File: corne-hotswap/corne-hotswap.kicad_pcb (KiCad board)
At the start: 2 copper layers, 133.8 x 91.7 mm, 49 parts, among them J1 Battery Connector, J2 nice!view, J3 USB_C_Receptacle_PowerOnly_6P, J4 Battery Wire, SW1 SW_Push, SW10 SW_Push, SW11 SW_Push, SW12 SW_Push, SW13 SW_Push, SW14 SW_Push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

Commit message: minor wiring update
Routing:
- net GND: track 99.1 -> 100.1 mm, vias 29 -> 30
- net battery: track 69.4 -> 68.9 mm

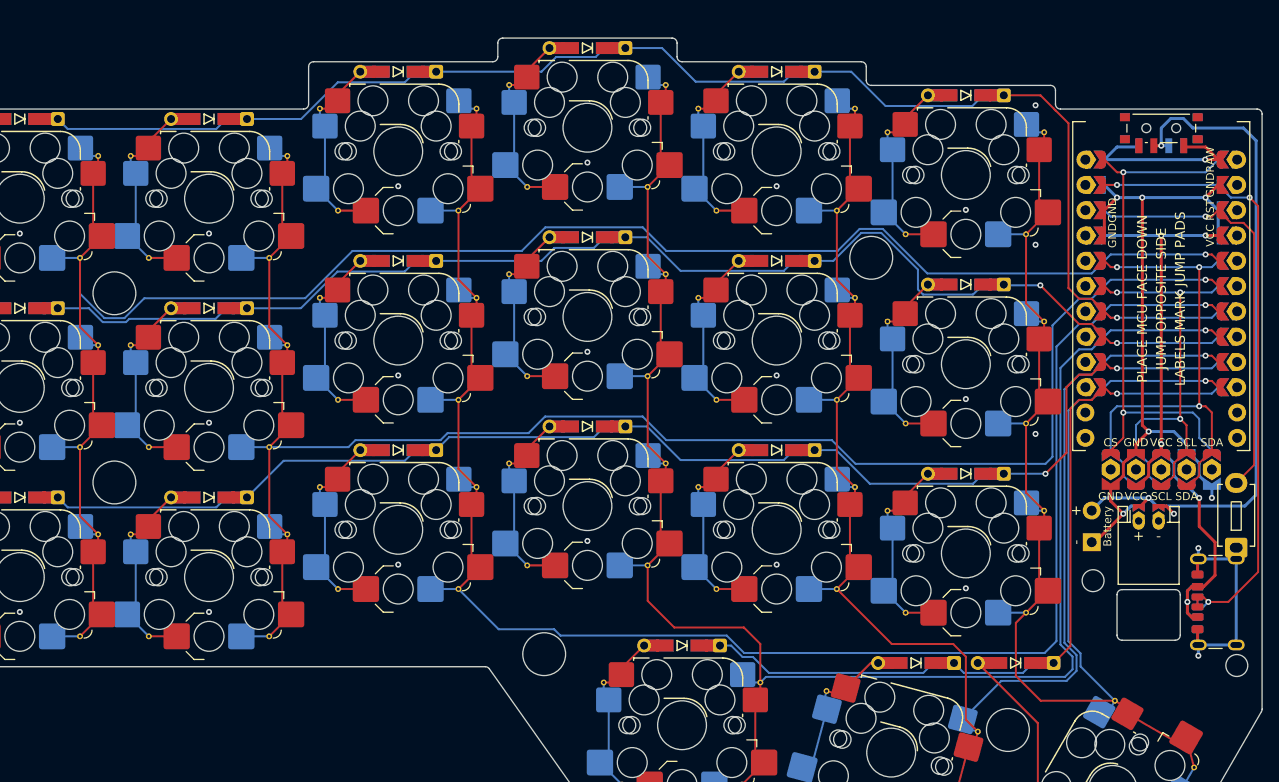
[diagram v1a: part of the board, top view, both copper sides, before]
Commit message: module wiring update
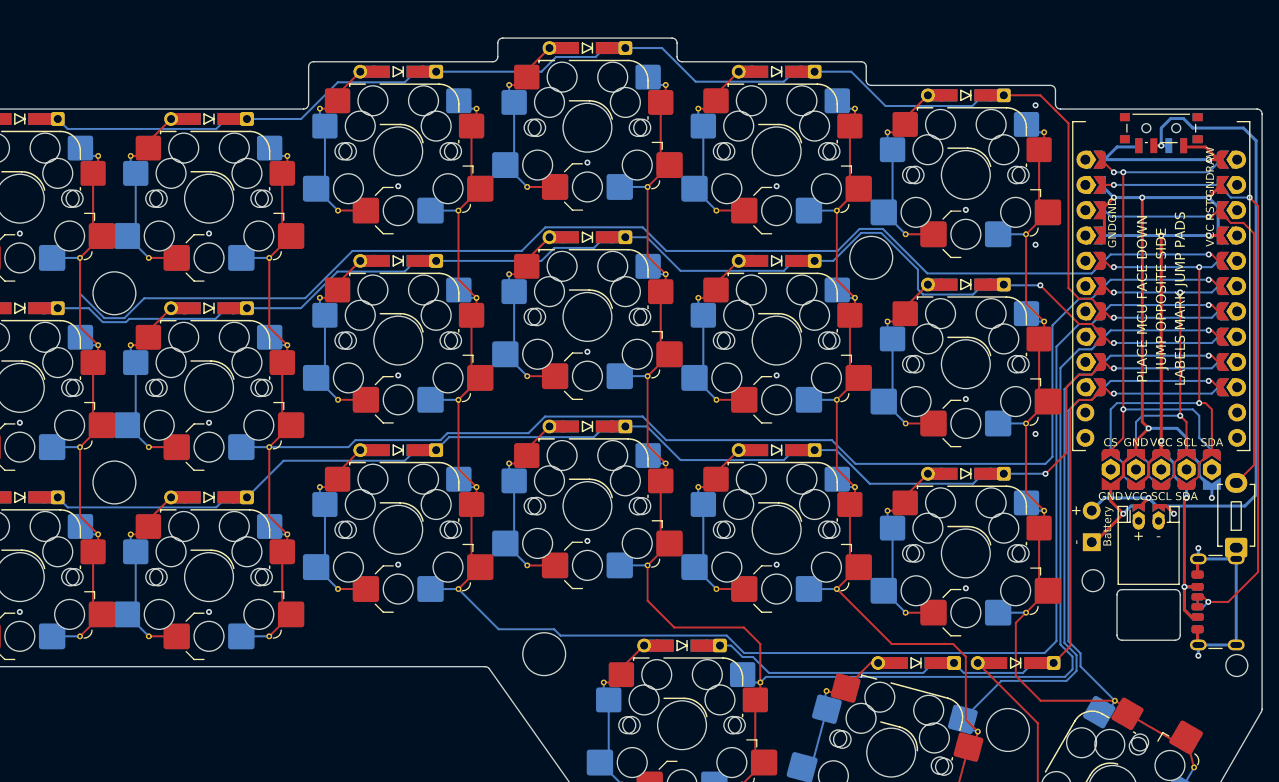
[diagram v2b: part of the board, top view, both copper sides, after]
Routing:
- net VCC: track 64.9 -> 64.2 mm
- net CS: track 52.5 -> 53.2 mm, vias 2 -> 3
- net GND: track 100.1 -> 100.7 mm
